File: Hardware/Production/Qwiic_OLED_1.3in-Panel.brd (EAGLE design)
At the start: 121.4 x 138.4 mm, 330 parts, among them J1 QWIIC_RIGHT_ANGLE, J10 QWIIC_RIGHT_ANGLE, J11 QWIIC_RIGHT_ANGLE, J13 QWIIC_RIGHT_ANGLE, J14 QWIIC_RIGHT_ANGLE, J16 QWIIC_RIGHT_ANGLE, J17 QWIIC_RIGHT_ANGLE, J19 QWIIC_RIGHT_ANGLE, J2 QWIIC_RIGHT_ANGLE, J20 QWIIC_RIGHT_ANGLE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

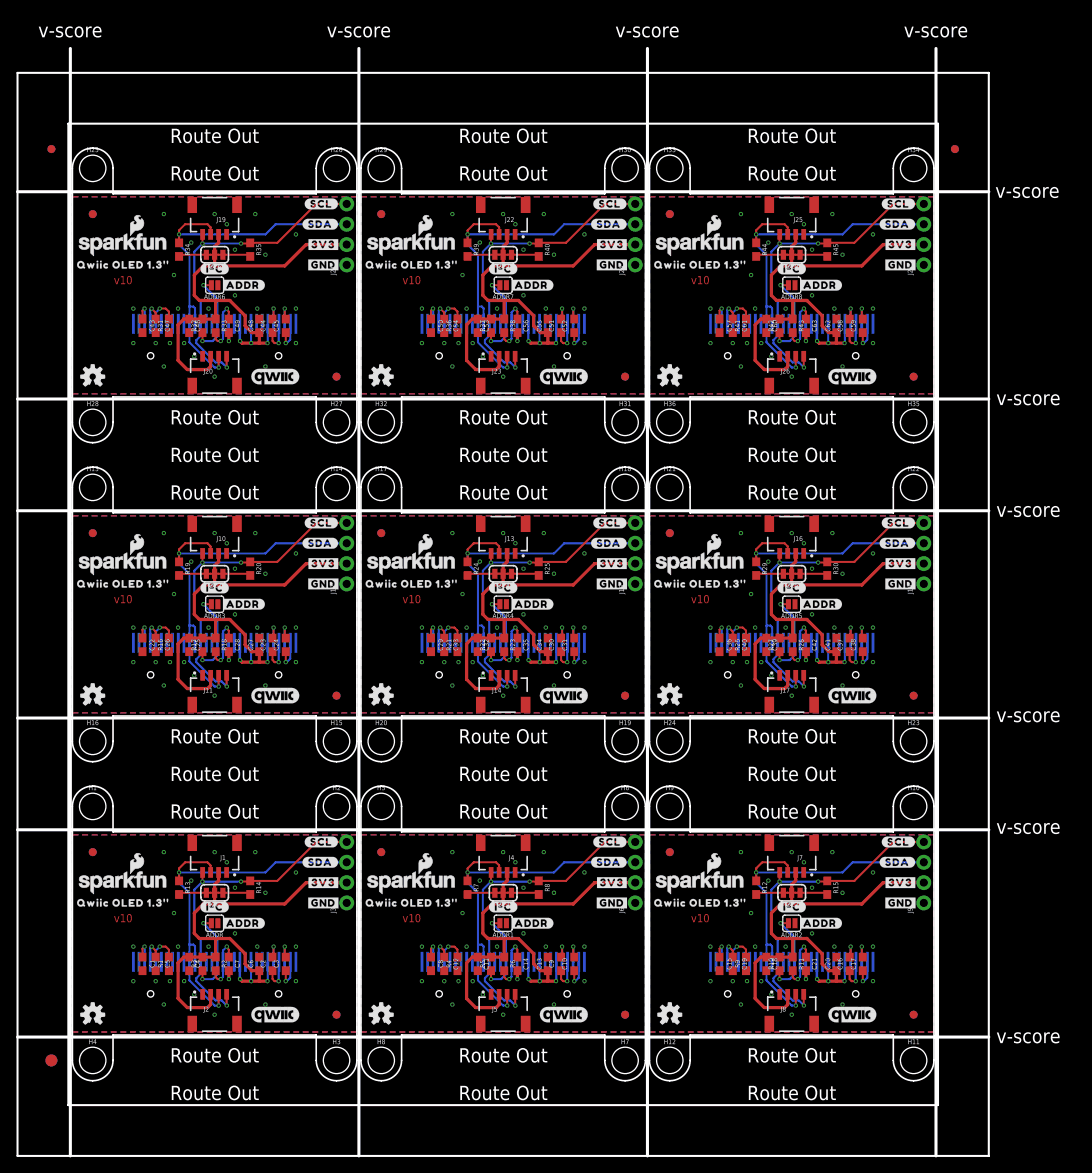
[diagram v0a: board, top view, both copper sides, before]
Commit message: Connect CS to GND
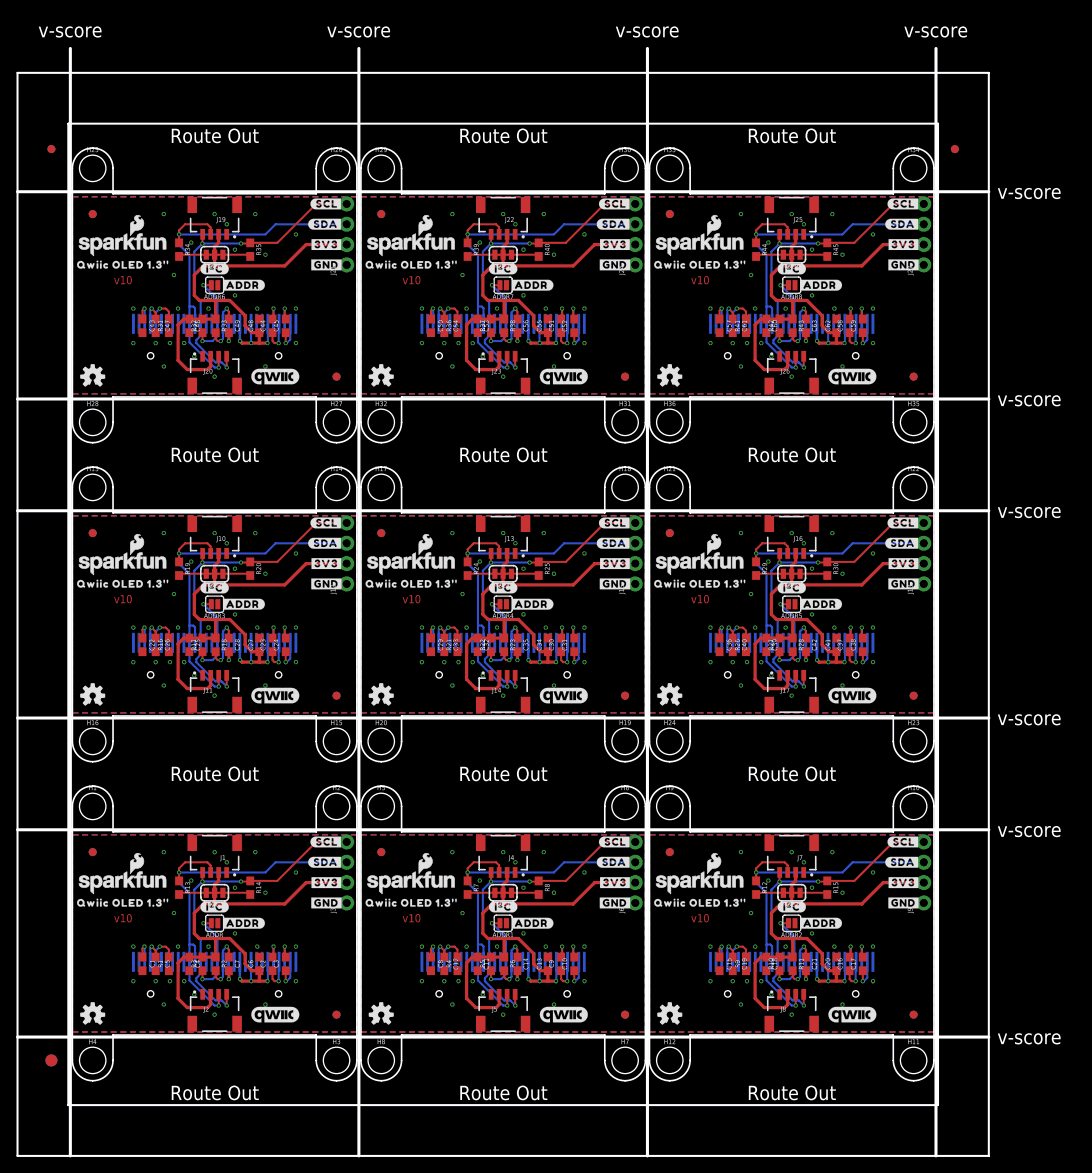
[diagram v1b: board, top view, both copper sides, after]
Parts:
- moved U$14 2.92 mm to (70.0, 27.3)
- moved U$21 2.92 mm to (106.0, 27.3)
- moved U$35 2.92 mm to (70.0, 67.2)
- moved U$42 2.92 mm to (106.0, 67.2)
- moved U$56 2.92 mm to (70.0, 107.1)
- moved U$63 2.92 mm to (106.0, 107.1)
- moved U$28 2.92 mm to (33.9, 67.2)
- moved U$49 2.92 mm to (33.9, 107.1)
- moved U$7 2.92 mm to (33.9, 27.3)
- moved U$27 2.79 mm to (33.9, 69.7)
- moved U$48 2.79 mm to (33.9, 109.6)
- moved U$6 2.79 mm to (33.9, 29.8)
- moved U$13 2.79 mm to (70.0, 29.8)
- moved U$20 2.79 mm to (106.0, 29.8)
- moved U$34 2.79 mm to (70.0, 69.7)
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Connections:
- net GND: now also OLED.13
- net GND1: now also OLED1.13
- net GND2: now also OLED2.13
- net GND3: now also OLED3.13
- net GND4: now also OLED4.13
- net GND5: now also OLED5.13
- net GND6: now also OLED6.13
- net GND7: now also OLED7.13
- net GND8: now also OLED8.13
